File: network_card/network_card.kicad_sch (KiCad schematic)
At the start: 27 parts, among them IC1 SN74HCT138N, IC2 SN74HCT138N, J1 Conn1, J2 INT_EN, J3 SPI_Header, U1 74HC04, U10 74LS08, U2 74HCT163E, U3 74LS32, U4 74LS08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

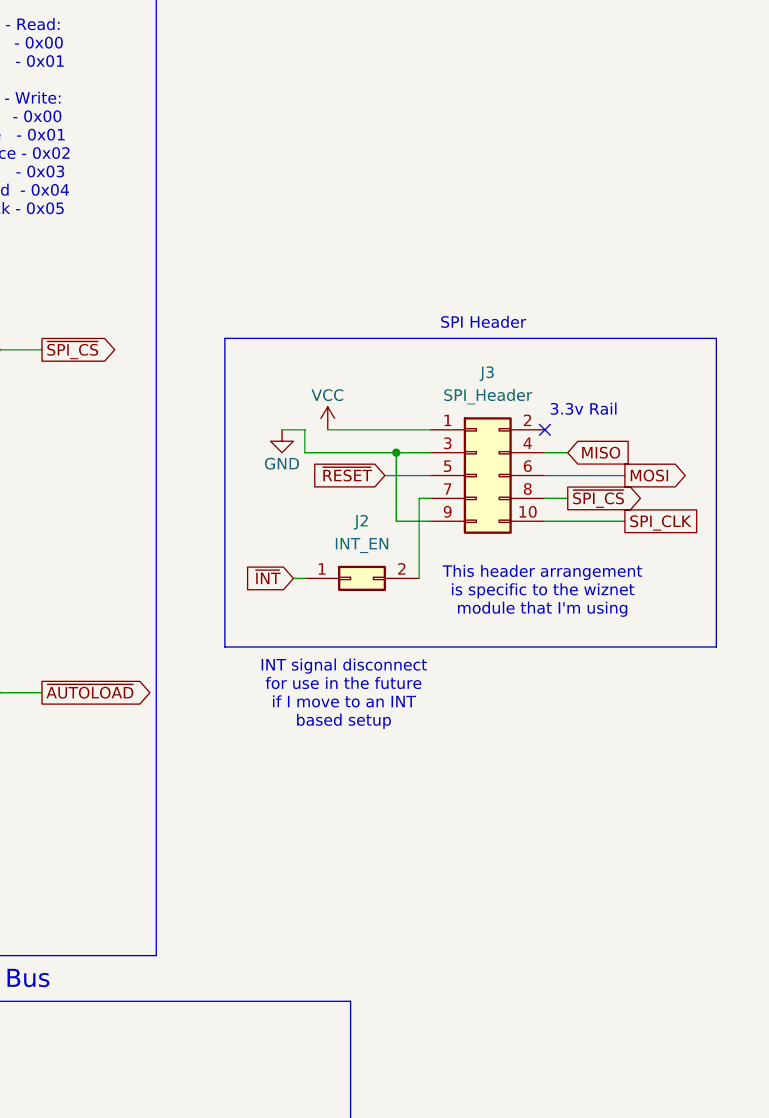
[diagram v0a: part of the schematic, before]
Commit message: Fixed misplacement of network module footprint. Added second footprint on edge of PCB for IDC connector
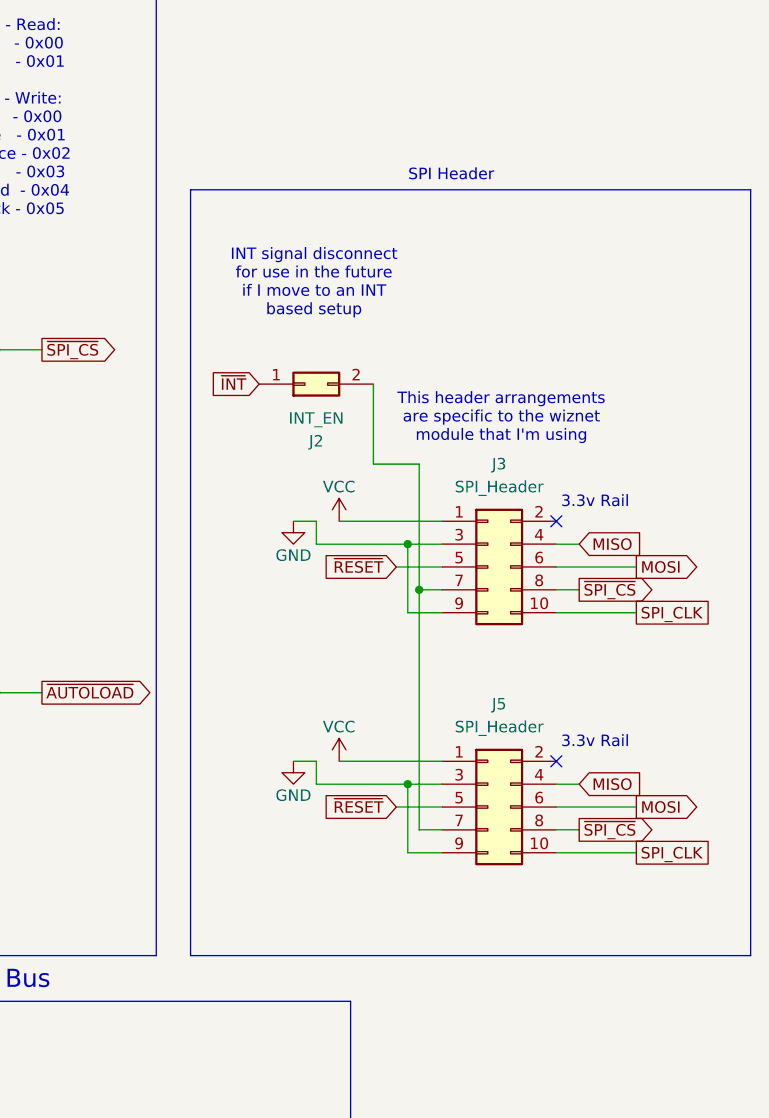
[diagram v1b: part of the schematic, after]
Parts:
- added J5: SPI_Header, Connector_IDC:IDC-Header_2x05_P2.54mm_Vertical, symbol Connector_Generic:Conn_02x05_Odd_Even
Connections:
- net GND: now also J5.3 (Pin_3), J5.9 (Pin_9)
- net MISO: now also J5.4 (Pin_4)
- net MOSI: now also J5.6 (Pin_6)
- net SPI_CLK: now also J5.10 (Pin_10)
- net VCC: now also J5.1 (Pin_1)
- net ~{RESET}: now also J5.5 (Pin_5)
- net ~{SPI_CS}: now also J5.8 (Pin_8)
- net at J2.2 (Pin_2), J3.7 (Pin_7): now also J5.7 (Pin_7)
- no-connect marks 55 -> 56
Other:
- note added: "This header arrangements are specific to the wiznet module that I'm using"
- note removed: "This header arrangement is specific to the wiznet module that I'm using"
- title: (none) -> Kludge Network Card
